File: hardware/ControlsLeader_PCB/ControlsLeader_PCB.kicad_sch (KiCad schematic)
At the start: 16 parts, among them J1 CarCANConnector_Out, J15 IgnConn_01x04, J16 SteeringConn_01x05, J17 Conn_01x02, J2 PeripheralCAN_out, J3 CarCANConnector_In, J4 PeripheralCAN_in, J6 Conn_2Rows-13Pins, J8 Dash_Lsom_Horn_Lights_PWR, U2 LeaderSOM

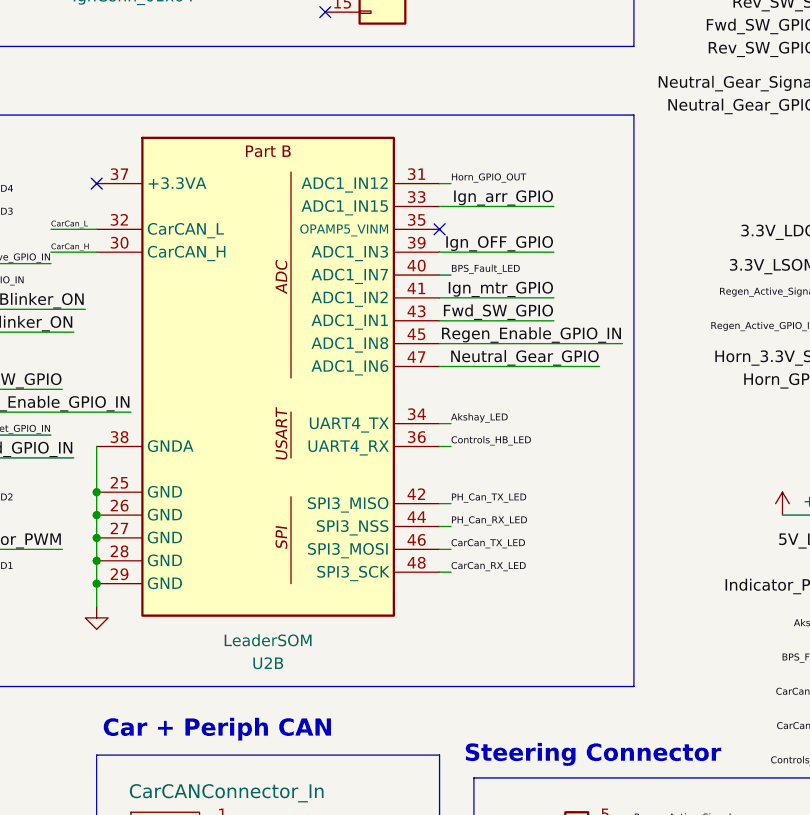
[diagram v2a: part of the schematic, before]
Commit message: Updated GPIO table, addressed lakshay review
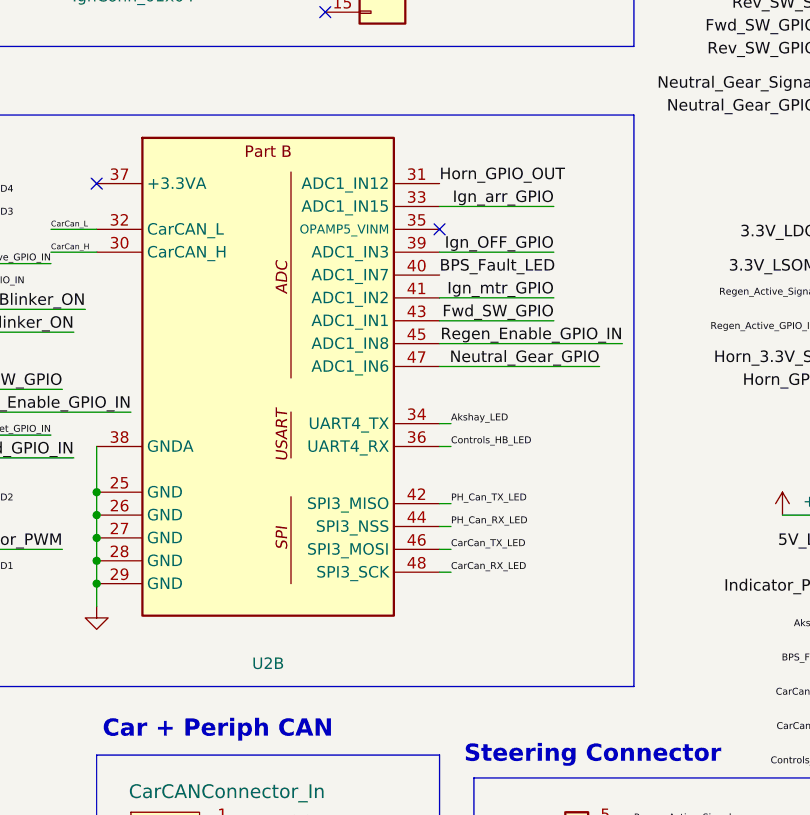
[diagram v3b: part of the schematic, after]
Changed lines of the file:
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@@
 	(wire
 		(pts
-			(xy 172.72 78.74) (xy 173.99 78.74)
-		)
-		(stroke
-			(width 0)
-			(type default)
-		)
-	)
-	(wire
-		(pts
 			(xy 190.5 179.07) (xy 198.12 179.07)
 		)
@@
 	(wire
 		(pts
-			(xy 172.72 68.58) (xy 173.99 68.58)
-		)
-		(stroke
-			(width 0)
-			(type default)
-		)
-	)
-	(wire
-		(pts
 			(xy 214.63 74.93) (xy 219.71 74.93)
 		)
@@
 				)
 			)
-			(table_cell "Horn_GPIO_OUT"
+			(table_cell "ACD1_IN12"
 				(exclude_from_sim no)
 				(at 16.51 162.56 0)
@@
 				)
 			)
-			(table_cell "GPIO_PC8"
+			(table_cell "GPIO_PB1"
 				(exclude_from_sim no)
 				(at 41.91 162.56 0)
@@
 				)
 			)
-			(table_cell "Ign_arr_GPIO"
+			(table_cell "ADC2_IN12"
 				(exclude_from_sim no)
 				(at 16.51 22.86 0)
@@
 				)
 			)
-			(table_cell "GPIO_PB12"
+			(table_cell "GPIO_PB2"
 				(exclude_from_sim no)
 				(at 41.91 22.86 0)
@@
 				)
 			)
-			(table_cell "Ign_mtr_GPIO"
+			(table_cell "ADC1_IN11"
 				(exclude_from_sim no)
 				(at 16.51 27.94 0)
@@
 				)
 			)
-			(table_cell "GPIO_PB13"
+			(table_cell "GPIO_PC1"
 				(exclude_from_sim no)
 				(at 41.91 27.94 0)
@@
 				)
 			)
-			(table_cell "Fwd_SW_GPIO"
+			(table_cell "ADC1_IN15"
 				(exclude_from_sim no)
 				(at 16.51 33.02 0)
@@
 				)
 			)
-			(table_cell "GPIO_PA10"
+			(table_cell "GPIO_PB0"
 				(exclude_from_sim no)
 				(at 41.91 33.02 0)
@@
 				)
 			)
-			(table_cell "Rev_SW_GPIO"
+			(table_cell "ADC1_IN3"
 				(exclude_from_sim no)
 				(at 16.51 38.1 0)
@@
 				)
 			)
-			(table_cell "GPIO_PB15"
+			(table_cell "GPIO_PA2"
 				(exclude_from_sim no)
 				(at 41.91 38.1 0)
@@
 				)
 			)
-			(table_cell "Neutral_Gear_GPIO"
+			(table_cell "ADC1_IN7"
 				(exclude_from_sim no)
 				(at 16.51 43.18 0)
@@
 				)
 			)
-			(table_cell "GPIO_PC11"
+			(table_cell "GPIO_PA6"
 				(exclude_from_sim no)
 				(at 41.91 43.18 0)
@@
 				)
 			)
-			(table_cell "Ign_OFF_GPIO"
+			(table_cell "ADC1_IN2"
 				(exclude_from_sim no)
 				(at 16.51 48.26 0)
@@
 				)
 			)
-			(table_cell "GPIO_PC10"
+			(table_cell "GPIO_PA1"
 				(exclude_from_sim no)
 				(at 41.91 48.26 0)
@@
 				)
 			)
-			(table_cell "Cruise_Set_GPIO_IN"
+			(table_cell "ADC1_IN1"
 				(exclude_from_sim no)
 				(at 16.51 53.34 0)
@@
 				)
 			)
-			(table_cell "GPIO_PC0"
+			(table_cell "GPIO_PA0"
 				(exclude_from_sim no)
 				(at 41.91 53.34 0)
@@
 				)
 			)
-			(table_cell "Cruise_Enable_GPIO_IN"
+			(table_cell "ADC1_IN8"
 				(exclude_from_sim no)
 				(at 16.51 58.42 0)
@@
 				)
 			)
-			(table_cell "GPIO_PC2"
+			(table_cell "GPIO_PA7"
 				(exclude_from_sim no)
 				(at 41.91 58.42 0)
@@
 				)
 			)
-			(table_cell "Regen_Enable_GPIO_IN"
+			(table_cell "ADC1_IN6"
 				(exclude_from_sim no)
 				(at 16.51 63.5 0)
@@
 				)
 			)
-			(table_cell "GPIO_PA0"
+			(table_cell "GPIO_PA5"
 				(exclude_from_sim no)
 				(at 41.91 63.5 0)
@@
 				)
 			)
-			(table_cell "Hazard_GPIO_IN"
+			(table_cell "UART5_TX"
 				(exclude_from_sim no)
 				(at 16.51 68.58 0)
@@
 				)
 			)
-			(table_cell "GPIO_PA1"
+			(table_cell "GPIO_PC12"
 				(exclude_from_sim no)
 				(at 41.91 68.58 0)
@@
 				)
 			)
-			(table_cell "Left_Blinker_ON"
+			(table_cell "UART5_RX"
 				(exclude_from_sim no)
 				(at 16.51 73.66 0)
@@
 				)
 			)
-			(table_cell "GPIO_PC1"
+			(table_cell "GPIO_PD2"
 				(exclude_from_sim no)
 				(at 41.91 73.66 0)
@@
 				)
 			)
-			(table_cell "Right_Blinker_ON"
+			(table_cell "USART1_TX"
 				(exclude_from_sim no)
 				(at 16.51 78.74 0)
@@
 				)
 			)
-			(table_cell "GPIO_PA2"
+			(table_cell "GPIO_PA9"
 				(exclude_from_sim no)
 				(at 41.91 78.74 0)
@@
 				)
 			)
-			(table_cell "Indicator_PWM"
+			(table_cell "USART1_RX"
 				(exclude_from_sim no)
 				(at 16.51 83.82 0)
@@
 				)
 			)
-			(table_cell "GPIO_PB0 (TIM1_CH2N)"
+			(table_cell "GPIO_PA10"
 				(exclude_from_sim no)
 				(at 41.91 83.82 0)
@@
 				)
 			)
-			(table_cell "Regen_Active_GPIO"
+			(table_cell "UART4_TX"
 				(exclude_from_sim no)
 				(at 16.51 88.9 0)
@@
 				)
 			)
-			(table_cell "GPIO_PB1"
+			(table_cell "GPIO_PC10"
 				(exclude_from_sim no)
 				(at 41.91 88.9 0)
@@
 				)
 			)
-			(table_cell "Extra_LED1"
+			(table_cell "UART4_RX"
 				(exclude_from_sim no)
 				(at 16.51 93.98 0)
@@
 				)
 			)
-			(table_cell "GPIO_PB2  "
+			(table_cell "GPIO_PC11"
 				(exclude_from_sim no)
 				(at 41.91 93.98 0)
@@
 				)
 			)
-			(table_cell "Extra_LED2"
+			(table_cell "I2C4_SDA"
 				(exclude_from_sim no)
 				(at 16.51 99.06 0)
@@
 				)
 			)
-			(table_cell "GPIO_PB12  "
+			(table_cell "GPIO_PC7"
 				(exclude_from_sim no)
 				(at 41.91 99.06 0)
@@
 				)
 			)
-			(table_cell "Extra_LED3"
+			(table_cell "I2C4_SCL"
 				(exclude_from_sim no)
 				(at 16.51 104.14 0)
@@
 				)
 			)
-			(table_cell "GPIO_PB10  "
+			(table_cell "GPIO_PC6"
 				(exclude_from_sim no)
 				(at 41.91 104.14 0)
@@
 				)
 			)
-			(table_cell "Akshay_LED"
+			(table_cell "I2C3_SDA"
 				(exclude_from_sim no)
 				(at 16.51 109.22 0)
@@
 				)
 			)
-			(table_cell "GPIO_PB11  "
+			(table_cell "GPIO_PC9"
 				(exclude_from_sim no)
 				(at 41.91 109.22 0)
@@
 				)
 			)
-			(table_cell "BPS_Fault_LED"
+			(table_cell "I2C3_SCL"
 				(exclude_from_sim no)
 				(at 16.51 114.3 0)
@@
 				)
 			)
-			(table_cell "GPIO_PC4  "
+			(table_cell "GPIO_PA8"
 				(exclude_from_sim no)
 				(at 41.91 114.3 0)
@@
 				)
 			)
-			(table_cell "CarCan_RX_LED"
+			(table_cell "SPI2_MISO"
 				(exclude_from_sim no)
 				(at 16.51 119.38 0)
@@
 				)
 			)
-			(table_cell "GPIO_PC5"
+			(table_cell "GPIO_PB14"
 				(exclude_from_sim no)
 				(at 41.91 119.38 0)
@@
 				)
 			)
-			(table_cell "CarCan_TX_LED"
+			(table_cell "SPI2_MOSI"
 				(exclude_from_sim no)
 				(at 16.51 124.46 0)
@@
 				)
 			)
-			(table_cell "GPIO_PC7  "
+			(table_cell "GPIO_PB15"
 				(exclude_from_sim no)
 				(at 41.91 124.46 0)
@@
 				)
 			)
-			(table_cell "Controls_HB_LED"
+			(table_cell "SPI2_SCK"
 				(exclude_from_sim no)
 				(at 16.51 129.54 0)
@@
 				)
 			)
-			(table_cell "GPIO_PC6  "
+			(table_cell "GPIO_PB13"
 				(exclude_from_sim no)
 				(at 41.91 129.54 0)
@@
 				)
 			)
-			(table_cell "PH_Can_RX_LED"
+			(table_cell "SPI3_MISO"
 				(exclude_from_sim no)
 				(at 16.51 134.62 0)
@@
 				)
 			)
-			(table_cell "GPIO_PC9  "
+			(table_cell "GPIO_PB4"
 				(exclude_from_sim no)
 				(at 41.91 134.62 0)
@@
 				)
 			)
-			(table_cell "Extra_LED4"
+			(table_cell "SPI3_NSS"
 				(exclude_from_sim no)
 				(at 16.51 139.7 0)
@@
 				)
 			)
-			(table_cell "GPIO_PB13"
+			(table_cell "GPIO_PA15"
 				(exclude_from_sim no)
 				(at 41.91 139.7 0)
@@
 				)
 			)
-			(table_cell "PH_Can_TX_LED"
+			(table_cell "SPI3_MOSI"
 				(exclude_from_sim no)
 				(at 16.51 144.78 0)
@@
 				)
 			)
-			(table_cell "GPIO_PB14"
+			(table_cell "GPIO_PB5"
 				(exclude_from_sim no)
 				(at 41.91 144.78 0)
@@
 				)
 			)
-			(table_cell "Horn_GPIO_IN"
+			(table_cell "SPI3_SCK"
 				(exclude_from_sim no)
 				(at 16.51 149.86 0)
@@
 				)
 			)
-			(table_cell "GPIO_PB15"
+			(table_cell "GPIO_PB3"
 				(exclude_from_sim no)
 				(at 41.91 149.86 0)
@@
 	)
 	(label "Horn_GPIO_OUT"
-		(at 173.99 68.58 0)
+		(at 172.72 68.58 0)
 		(effects
 			(font
-				(size 0.762 0.762)
+				(size 1.27 1.27)
 			)
 			(justify left bottom)
@@
 	)
 	(label "BPS_Fault_LED"
-		(at 173.99 78.74 0)
+		(at 172.72 78.74 0)
 		(effects
 			(font
-				(size 0.762 0.762)
+				(size 1.27 1.27)
 			)
 			(justify left bottom)
@@
 					(size 1.27 1.27)
 				)
+				(hide yes)
 			)
 		)

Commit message: Final reviews addressed - RevA
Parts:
- added D28, D30: Controls_Leader_Status_Red, LED_SMD:LED_0603_1608Metric_Pad1.05x0.95mm_HandSolder, symbol Device:LED
- added R10, R56: 1.1k, Capacitor_SMD:C_0603_1608Metric_Pad1.08x0.95mm_HandSolder, symbol Device:R
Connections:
- net 3.3V_LDO: now also D30.2 (A)
- net 5V_LDO: now also D28.2 (A)
- net GND: now also R10.2, R56.2; no longer U2.38 (GNDA)
- new net: D30.1 (K), R56.1
- new net: D28.1 (K), R10.1
- no-connect marks 6 -> 7
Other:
- moved on the sheet: F1

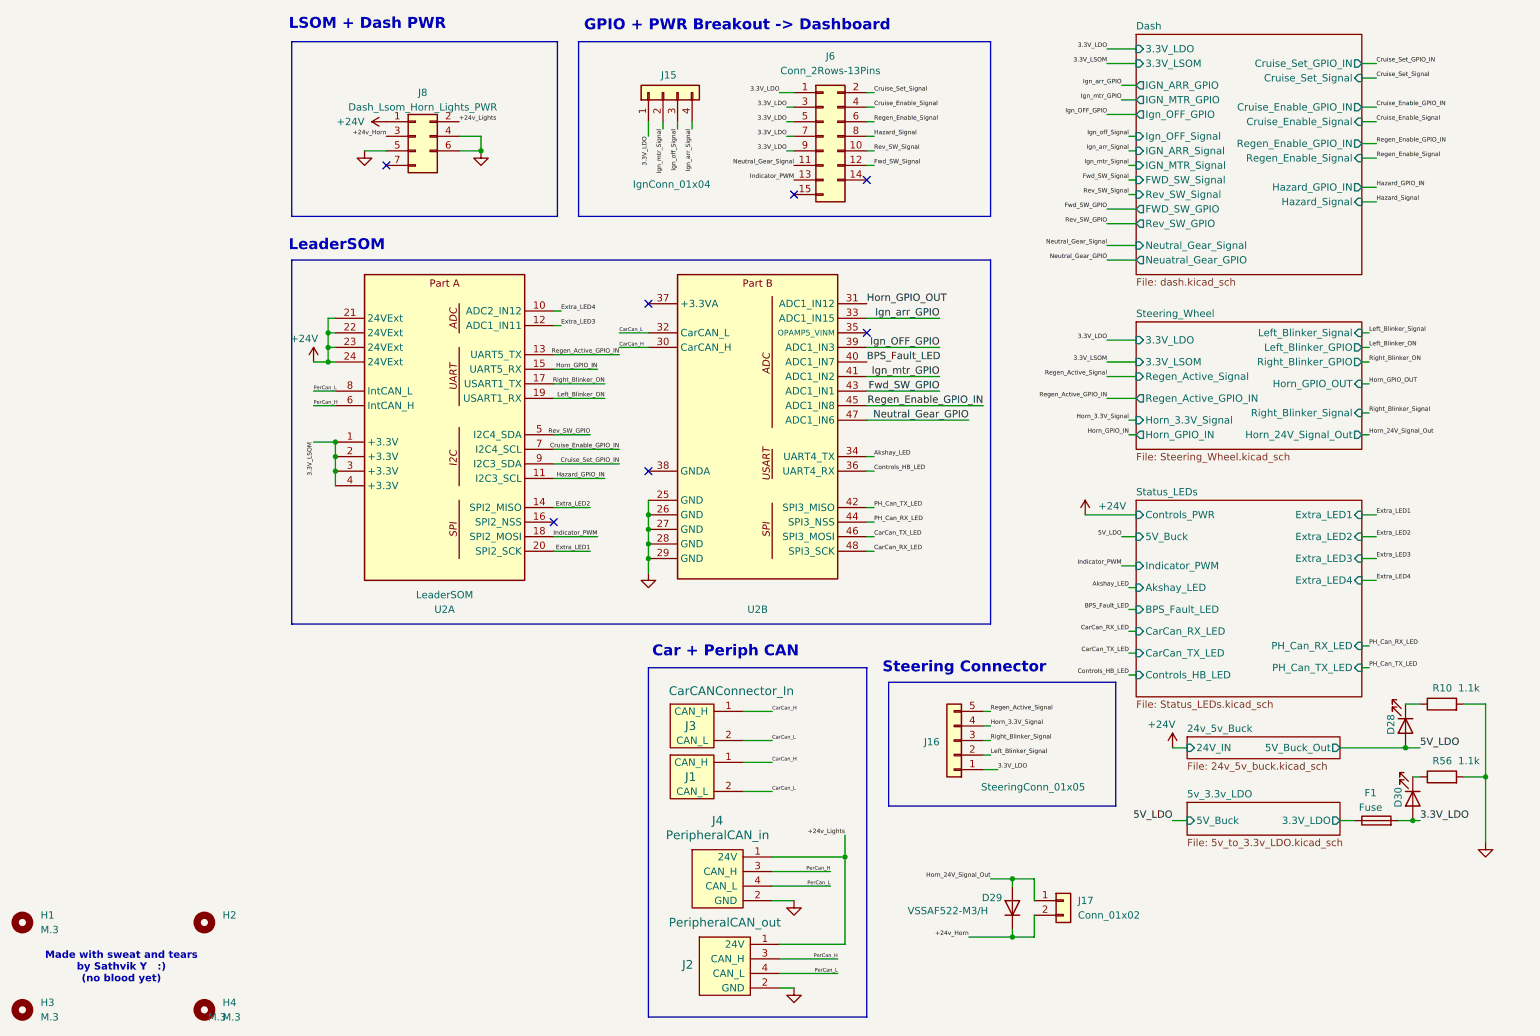
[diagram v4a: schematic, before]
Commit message: Fixed DRC errors, and indicator switch pwr/pwm output conn to steering
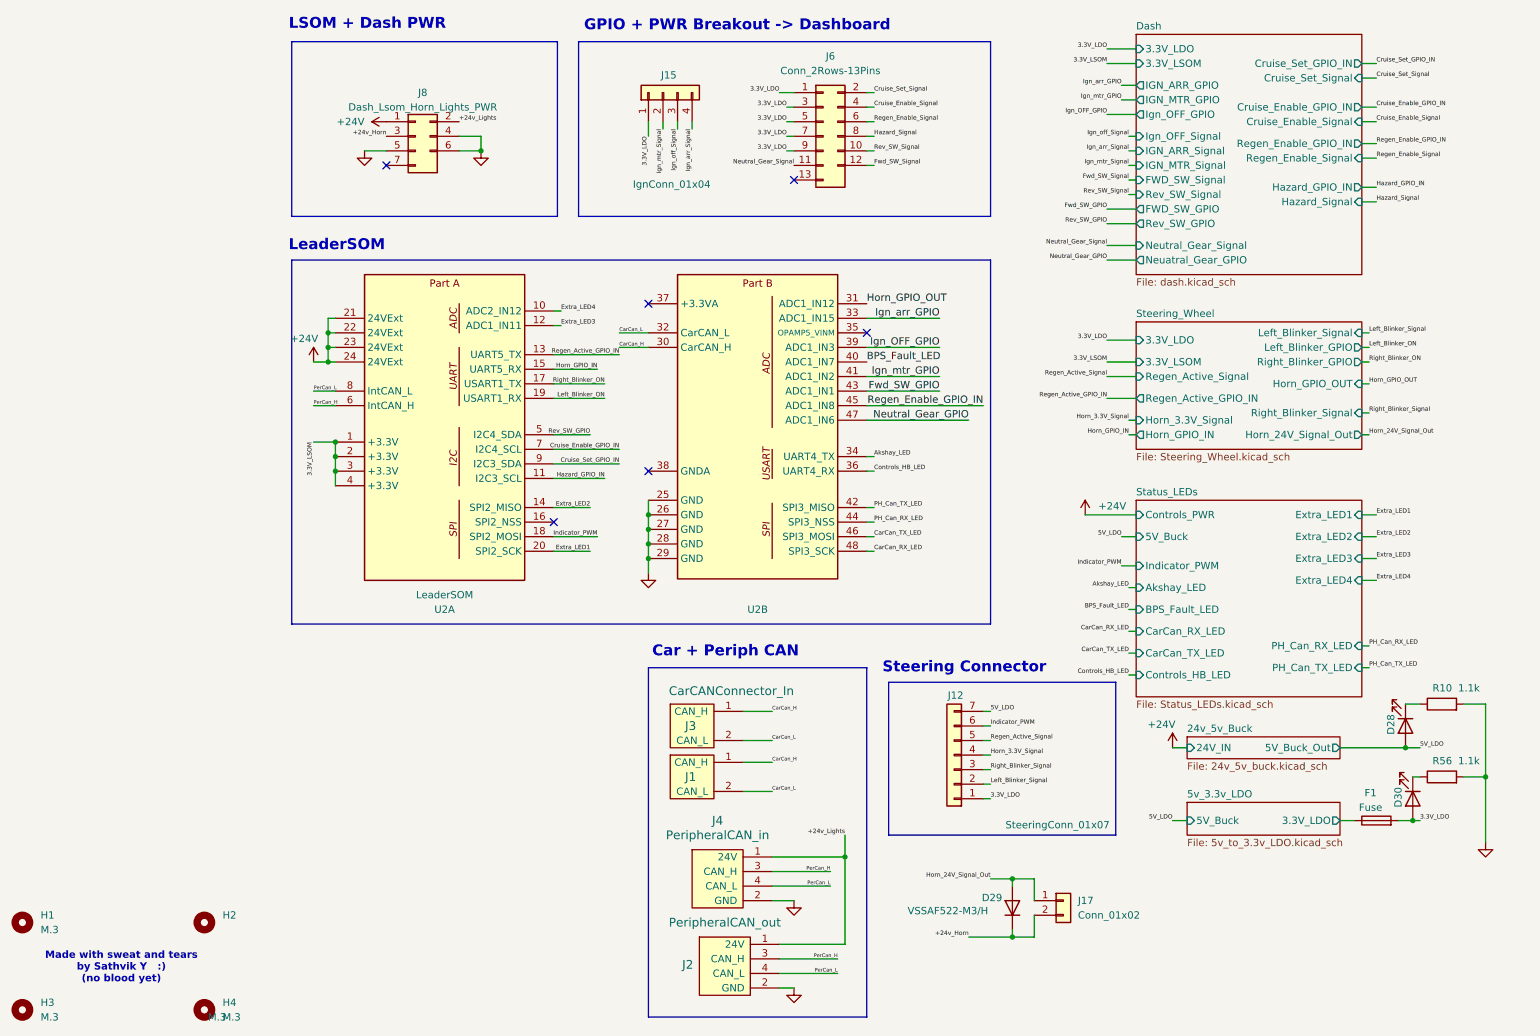
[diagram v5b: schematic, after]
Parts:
- removed J16: SteeringConn_01x05, Connector_Molex:Molex_Nano-Fit_105313-xx05_1x05_P2.50mm_Horizontal, symbol Connector_Generic:Conn_01x05
- removed J6: Conn_2Rows-13Pins, Connector_Molex:Molex_Nano-Fit_105314-xx14_2x07_P2.50mm_Horizontal, symbol Connector_Generic:Conn_2Rows-15Pins
- added J12: SteeringConn_01x07, Connector_Molex:Molex_Nano-Fit_105313-xx07_1x07_P2.50mm_Horizontal, symbol Connector_Generic:Conn_01x07
- added J6: Conn_2Rows-13Pins, Connector_Molex:Molex_Nano-Fit_105314-xx12_2x06_P2.50mm_Horizontal, symbol Connector_Generic:Conn_2Rows-13Pins
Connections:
- net 3.3V_LDO: now also J12.1 (Pin_1), J6.1 (Pin_1), J6.3 (Pin_3), J6.5 (Pin_5), J6.7 (Pin_7), J6.9 (Pin_9)
- net 5V_LDO: now also J12.7 (Pin_7)
- net Cruise_Enable_Signal: now also J6.4 (Pin_4)
- net Cruise_Set_Signal: now also J6.2 (Pin_2)
- net Fwd_SW_Signal: now also J6.12 (Pin_12)
- net Hazard_Signal: now also J6.8 (Pin_8)
- net Horn_3.3V_Signal: now also J12.4 (Pin_4)
- net Indicator_PWM: now also J12.6 (Pin_6)
- net Left_Blinker_Signal: now also J12.2 (Pin_2)
- net Neutral_Gear_Signal: now also J6.11 (Pin_11)
- net Regen_Active_Signal: now also J12.5 (Pin_5)
- net Regen_Enable_Signal: now also J6.6 (Pin_6)
- net Rev_SW_Signal: now also J6.10 (Pin_10)
- net Right_Blinker_Signal: now also J12.3 (Pin_3)
- no-connect marks 7 -> 6
